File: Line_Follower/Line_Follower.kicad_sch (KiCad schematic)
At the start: 24 parts, among them J1 Battery terminal, J10 Motor_B, J11 8-Channel IR Array, J9 Motor_A, SW1 Slide Switch, SW3 Mode, SW6 Calibration, U1 ESP32-DEVKITC, U2 LM2596 Buck Converter, U3 TB6612FNG_MD

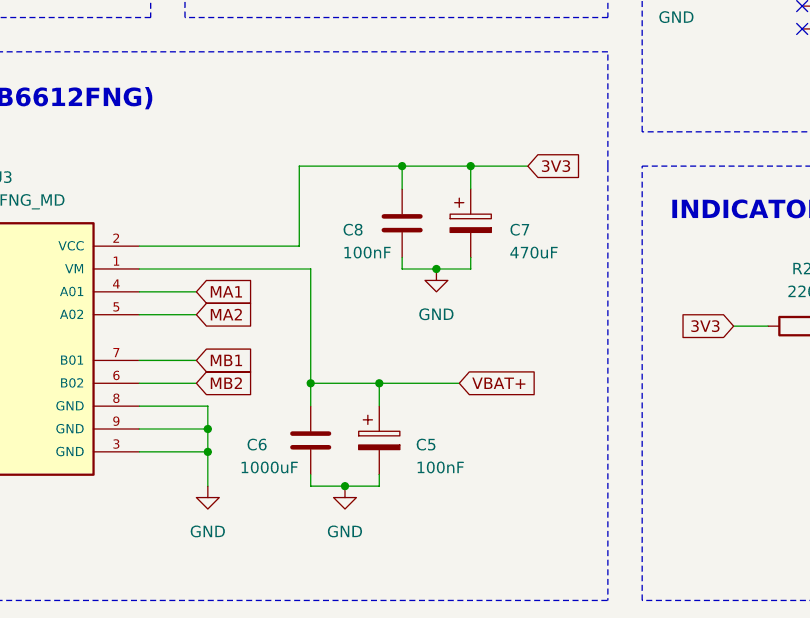
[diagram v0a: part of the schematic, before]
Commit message: Capacitors removed
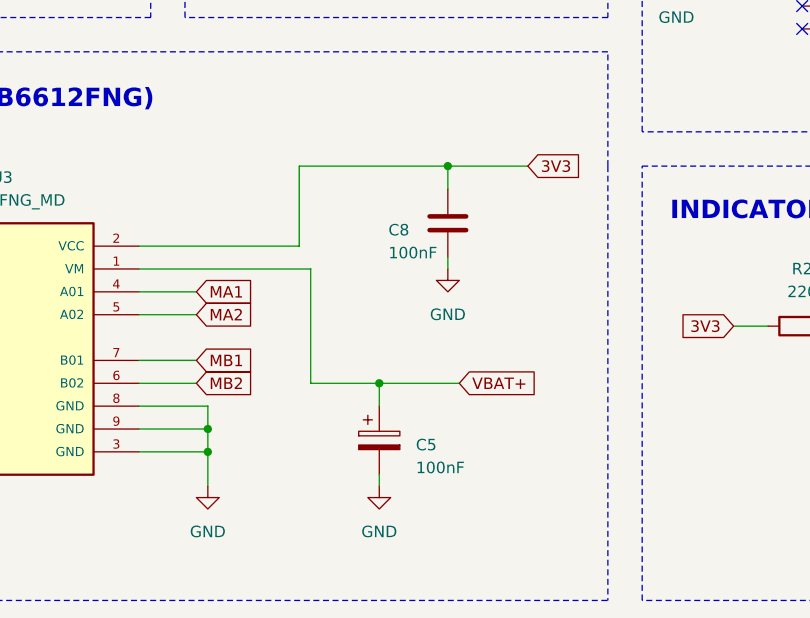
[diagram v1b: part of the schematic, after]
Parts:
- removed C6: 1000uF, Capacitors:CAPPRD750W80D1600H2500, symbol Device:C
- removed C7: 470uF, Capacitors:CAPPRD750W80D1600H2500, symbol Device:C_Polarized
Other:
- moved on the sheet: C8
